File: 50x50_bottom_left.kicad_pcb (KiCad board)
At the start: 2 copper layers, 48.9 x 48.3 mm, 103 parts, among them CON1 BARREL_JACK, J1 INTERCONNECT_1X03, J10 INTERCONNECT_1X03, J11 INTERCONNECT_1X03, J12 INTERCONNECT_1X03, J13 INTERCONNECT_1X03, J14 INTERCONNECT_1X03, J15 INTERCONNECT_1X03, J16 INTERCONNECT_1X03, J17 INTERCONNECT_1X03, J18 INTERCONNECT_1X03, J19 INTERCONNECT_1X03, J2 INTERCONNECT_1X03, J20 INTERCONNECT_1X03, J21 INTERCONNECT_1X03, J22 INTERCONNECT_1X03, J23 INTERCONNECT_1X03, J24 INTERCONNECT_1X03, J25 INTERCONNECT_1X03, J26 INTERCONNECT_1X03, J27 INTERCONNECT_1X03, J28 INTERCONNECT_1X03, J29 INTERCONNECT_1X03, J3 INTERCONNECT_1X03, J30 INTERCONNECT_1X03, J31 INTERCONNECT_1X03, J32 INTERCONNECT_1X03, J33 INTERCONNECT_1X03, J34 INTERCONNECT_1X03, J35 INTERCONNECT_1X03, J36 INTERCONNECT_1X03, J37 INTERCONNECT_1X03, J38 INTERCONNECT_1X03, J39 INTERCONNECT_1X03, J4 INTERCONNECT_1X03, J40 INTERCONNECT_1X03, J41 INTERCONNECT_1X03, J42 INTERCONNECT_1X03, J43 INTERCONNECT_1X03, J44 INTERCONNECT_1X03, J45 INTERCONNECT_1X03, J46 INTERCONNECT_1X03, J47 INTERCONNECT_1X03, J48 INTERCONNECT_1X03, J49 INTERCONNECT_1X03, J5 INTERCONNECT_1X03, J50 INTERCONNECT_1X03, J51 INTERCONNECT_1X03, J52 INTERCONNECT_1X03, J53 INTERCONNECT_1X03, J54 INTERCONNECT_1X03, J55 INTERCONNECT_1X03, J56 INTERCONNECT_1X03, J57 INTERCONNECT_1X03, J58 INTERCONNECT_1X03, J59 INTERCONNECT_1X03, J6 INTERCONNECT_1X03, J60 INTERCONNECT_1X03, J61 INTERCONNECT_1X03, J62 INTERCONNECT_1X03, J63 INTERCONNECT_1X03, J64 INTERCONNECT_1X03, J65 INTERCONNECT_1X02, J7 INTERCONNECT_1X03, J8 INTERCONNECT_1X03, J9 INTERCONNECT_1X03, P1 CONN_8X2, P2 CONN_8X2, U1 LM7805CT

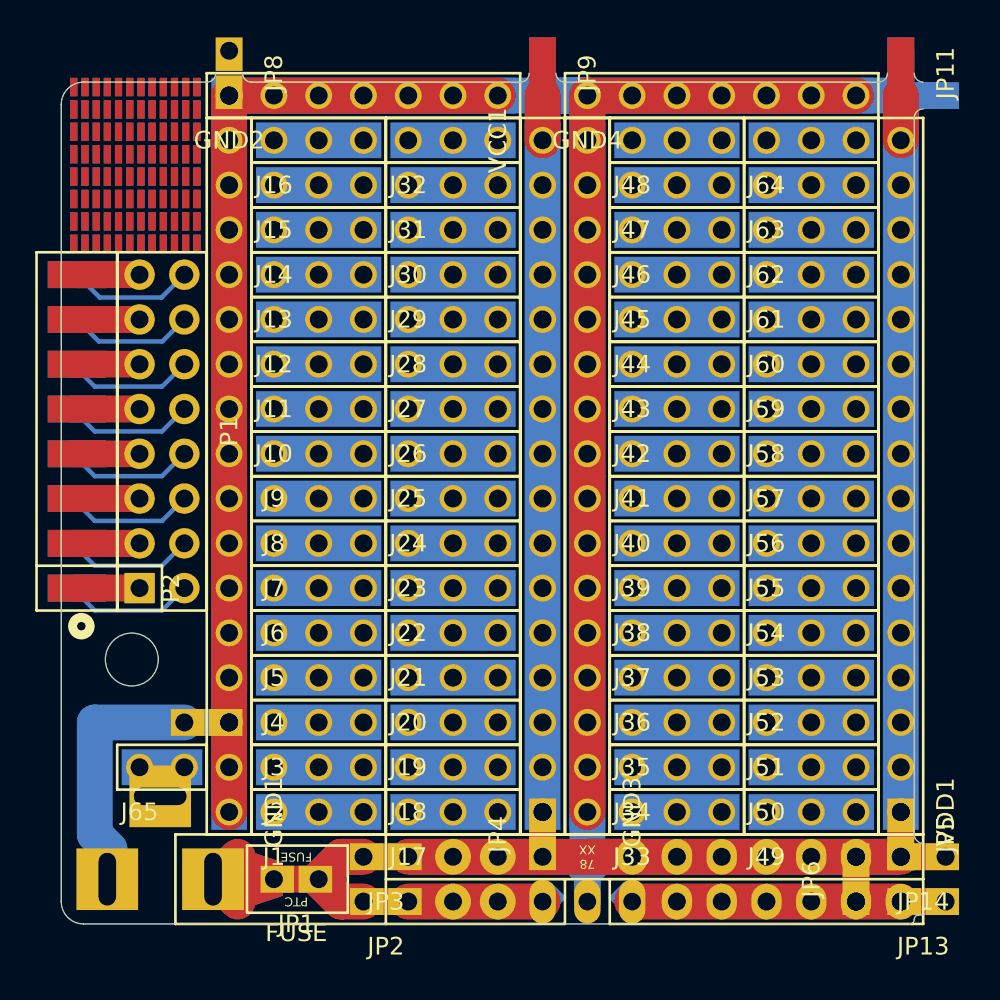
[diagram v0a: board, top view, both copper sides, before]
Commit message: added 3*3 mouse bites between the sub-boards on both edges
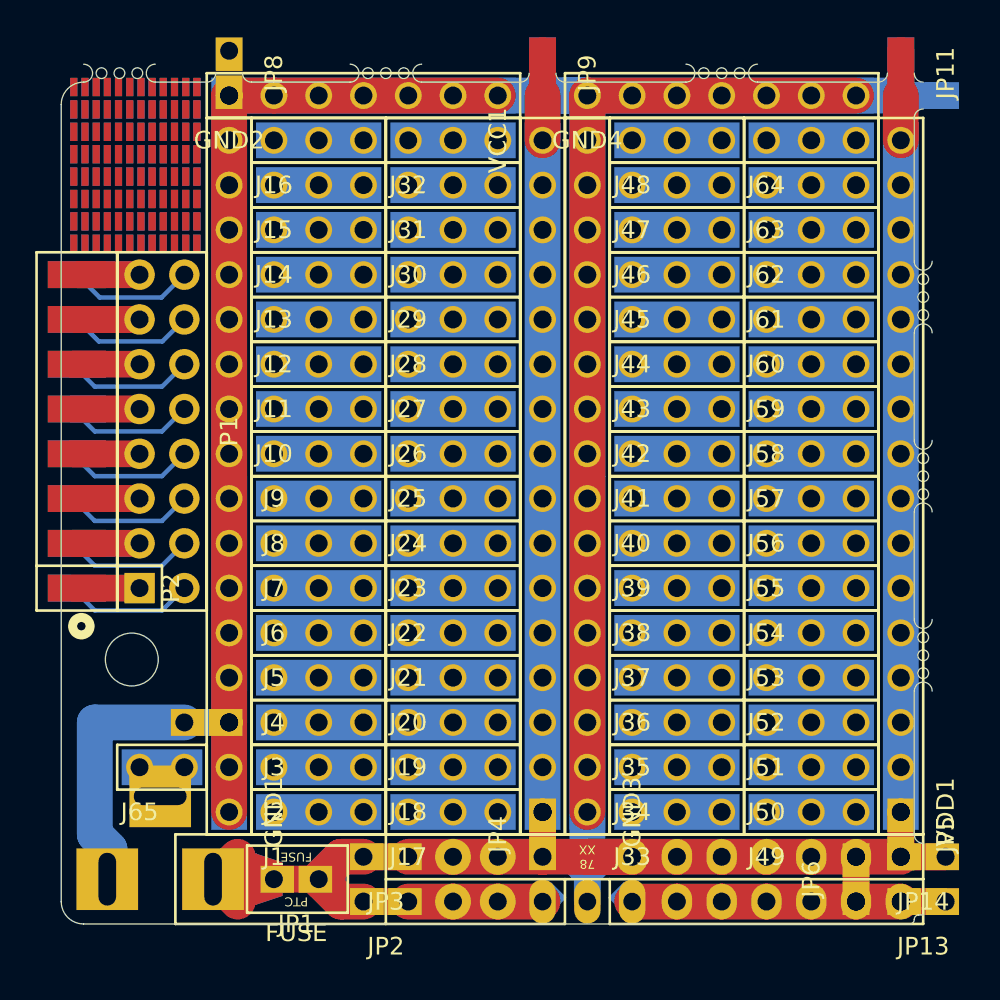
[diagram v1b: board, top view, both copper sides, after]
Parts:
- added Mouse_Bites_3_1.27mm: VAL**, Misc:Mouse_Bites_3_1.016mm, F.Cu at (44.8, 29.2)
- added Mouse_Bites_3_1.27mm: VAL**, Misc:Mouse_Bites_3_1.016mm, F.Cu at (91.4, 63.2)
- added Mouse_Bites_3_1.27mm: VAL**, Misc:Mouse_Bites_3_1.016mm, F.Cu at (91.4, 53.1)
- added Mouse_Bites_3_1.27mm: VAL**, Misc:Mouse_Bites_3_1.016mm, F.Cu at (91.4, 42.9)
- added Mouse_Bites_3_1.27mm: VAL**, Misc:Mouse_Bites_3_1.016mm, F.Cu at (79.0, 29.2)
- added Mouse_Bites_3_1.27mm: VAL**, Misc:Mouse_Bites_3_1.016mm, F.Cu at (59.9, 29.2)
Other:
- outline, holes or cut-outs redrawn
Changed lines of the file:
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@@
     (links 341)
     (no_connects 6)
-    (area 34.144048 26.7335 95.967572 82.309)
+    (area 34.144048 26.231 98.754715 82.309)
     (thickness 1.6)
-    (drawings 54)
+    (drawings 59)
     (tracks 88)
     (zones 0)
-    (modules 103)
+    (modules 109)
     (nets 99)
   )
@@
     (mod_text_size 1 1)
     (mod_text_width 0.15)
-    (pad_size 1.7272 2.032)
-    (pad_drill 1.016)
+    (pad_size 0.6096 0.6096)
+    (pad_drill 0.6096)
     (pad_to_mask_clearance 0)
     (aux_axis_origin 0 0)
@@
     )
   )
+  (module Misc:Mouse_Bites_3_1.016mm (layer F.Cu)
+    (at 44.831 29.21)
+    (fp_text reference Mouse_Bites_3_1.27mm (at 0 -1.8) (layer F.SilkS) hide
+      (effects (font (size 1 1) (thickness 0.15)))
+    )
+    (fp_text value VAL** (at 0 1.55) (layer F.SilkS) hide
+      (effects (font (size 1 1) (thickness 0.15)))
+    )
+    (fp_arc (start -1.016 0) (end -1.016 -0.508) (angle 180) (layer Edge.Cuts) (width 0.0254))
+    (fp_arc (start 3.048 0) (end 3.048 0.508) (angle 180) (layer Edge.Cuts) (width 0.0254))
+    (pad "" np_thru_hole circle (at 2.032 0) (size 0.6096 0.6096) (drill 0.6096) (layers *.Cu *.Mask F.SilkS)
+      (clearance 0.2032))
+    (pad "" np_thru_hole circle (at 1.016 0) (size 0.6096 0.6096) (drill 0.6096) (layers *.Cu *.Mask F.SilkS)
+      (clearance 0.2032))
+    (pad "" np_thru_hole circle (at 0 0) (size 0.6096 0.6096) (drill 0.6096) (layers *.Cu *.Mask F.SilkS)
+      (clearance 0.2032))
+  )
+  (module Misc:Mouse_Bites_3_1.016mm (layer F.Cu)
+    (at 91.44 63.246 90)
+    (fp_text reference Mouse_Bites_3_1.27mm (at 0 -1.8 90) (layer F.SilkS) hide
+      (effects (font (size 1 1) (thickness 0.15)))
+    )
+    (fp_text value VAL** (at 0 1.55 90) (layer F.SilkS) hide
+      (effects (font (size 1 1) (thickness 0.15)))
+    )
+    (fp_arc (start -1.016 0) (end -1.016 -0.508) (angle 180) (layer Edge.Cuts) (width 0.0254))
+    (fp_arc (start 3.048 0) (end 3.048 0.508) (angle 180) (layer Edge.Cuts) (width 0.0254))
+    (pad "" np_thru_hole circle (at 2.032 0 90) (size 0.6096 0.6096) (drill 0.6096) (layers *.Cu *.Mask F.SilkS)
+      (clearance 0.2032))
+    (pad "" np_thru_hole circle (at 1.016 0 90) (size 0.6096 0.6096) (drill 0.6096) (layers *.Cu *.Mask F.SilkS)
+      (clearance 0.2032))
+    (pad "" np_thru_hole circle (at 0 0 90) (size 0.6096 0.6096) (drill 0.6096) (layers *.Cu *.Mask F.SilkS)
+      (clearance 0.2032))
+  )
+  (module Misc:Mouse_Bites_3_1.016mm (layer F.Cu)
+    (at 91.44 53.086 90)
+    (fp_text reference Mouse_Bites_3_1.27mm (at 0 -1.8 90) (layer F.SilkS) hide
+      (effects (font (size 1 1) (thickness 0.15)))
+    )
+    (fp_text value VAL** (at 0 1.55 90) (layer F.SilkS) hide
+      (effects (font (size 1 1) (thickness 0.15)))
+    )
+    (fp_arc (start -1.016 0) (end -1.016 -0.508) (angle 180) (layer Edge.Cuts) (width 0.0254))
+    (fp_arc (start 3.048 0) (end 3.048 0.508) (angle 180) (layer Edge.Cuts) (width 0.0254))
+    (pad "" np_thru_hole circle (at 2.032 0 90) (size 0.6096 0.6096) (drill 0.6096) (layers *.Cu *.Mask F.SilkS)
+      (clearance 0.2032))
+    (pad "" np_thru_hole circle (at 1.016 0 90) (size 0.6096 0.6096) (drill 0.6096) (layers *.Cu *.Mask F.SilkS)
+      (clearance 0.2032))
+    (pad "" np_thru_hole circle (at 0 0 90) (size 0.6096 0.6096) (drill 0.6096) (layers *.Cu *.Mask F.SilkS)
+      (clearance 0.2032))
+  )
+  (module Misc:Mouse_Bites_3_1.016mm (layer F.Cu)
+    (at 91.44 42.926 90)
+    (fp_text reference Mouse_Bites_3_1.27mm (at 0 -1.8 90) (layer F.SilkS) hide
+      (effects (font (size 1 1) (thickness 0.15)))
+    )
+    (fp_text value VAL** (at 0 1.55 90) (layer F.SilkS) hide
+      (effects (font (size 1 1) (thickness 0.15)))
+    )
+    (fp_arc (start -1.016 0) (end -1.016 -0.508) (angle 180) (layer Edge.Cuts) (width 0.0254))
+    (fp_arc (start 3.048 0) (end 3.048 0.508) (angle 180) (layer Edge.Cuts) (width 0.0254))
+    (pad "" np_thru_hole circle (at 2.032 0 90) (size 0.6096 0.6096) (drill 0.6096) (layers *.Cu *.Mask F.SilkS)
+      (clearance 0.2032))
+    (pad "" np_thru_hole circle (at 1.016 0 90) (size 0.6096 0.6096) (drill 0.6096) (layers *.Cu *.Mask F.SilkS)
+      (clearance 0.2032))
+    (pad "" np_thru_hole circle (at 0 0 90) (size 0.6096 0.6096) (drill 0.6096) (layers *.Cu *.Mask F.SilkS)
+      (clearance 0.2032))
+  )
+  (module Misc:Mouse_Bites_3_1.016mm (layer F.Cu)
+    (at 78.994 29.21)
+    (fp_text reference Mouse_Bites_3_1.27mm (at 0 -1.8) (layer F.SilkS) hide
+      (effects (font (size 1 1) (thickness 0.15)))
+    )
+    (fp_text value VAL** (at 0 1.55) (layer F.SilkS) hide
+      (effects (font (size 1 1) (thickness 0.15)))
+    )
+    (fp_arc (start -1.016 0) (end -1.016 -0.508) (angle 180) (layer Edge.Cuts) (width 0.0254))
+    (fp_arc (start 3.048 0) (end 3.048 0.508) (angle 180) (layer Edge.Cuts) (width 0.0254))
+    (pad "" np_thru_hole circle (at 2.032 0) (size 0.6096 0.6096) (drill 0.6096) (layers *.Cu *.Mask F.SilkS)
+      (clearance 0.2032))
+    (pad "" np_thru_hole circle (at 1.016 0) (size 0.6096 0.6096) (drill 0.6096) (layers *.Cu *.Mask F.SilkS)
+      (clearance 0.2032))
+    (pad "" np_thru_hole circle (at 0 0) (size 0.6096 0.6096) (drill 0.6096) (layers *.Cu *.Mask F.SilkS)
+      (clearance 0.2032))
+  )
+  (module Misc:Mouse_Bites_3_1.016mm (layer F.Cu)
+    (at 59.944 29.21)
+    (fp_text reference Mouse_Bites_3_1.27mm (at 0 -1.8) (layer F.SilkS) hide
+      (effects (font (size 1 1) (thickness 0.15)))
+    )
+    (fp_text value VAL** (at 0 1.55) (layer F.SilkS) hide
+      (effects (font (size 1 1) (thickness 0.15)))
+    )
+    (fp_arc (start -1.016 0) (end -1.016 -0.508) (angle 180) (layer Edge.Cuts) (width 0.0254))
+    (fp_arc (start 3.048 0) (end 3.048 0.508) (angle 180) (layer Edge.Cuts) (width 0.0254))
+    (pad "" np_thru_hole circle (at 2.032 0) (size 0.6096 0.6096) (drill 0.6096) (layers *.Cu *.Mask F.SilkS)
+      (clearance 0.2032))
+    (pad "" np_thru_hole circle (at 1.016 0) (size 0.6096 0.6096) (drill 0.6096) (layers *.Cu *.Mask F.SilkS)
+      (clearance 0.2032))
+    (pad "" np_thru_hole circle (at 0 0) (size 0.6096 0.6096) (drill 0.6096) (layers *.Cu *.Mask F.SilkS)
+      (clearance 0.2032))
+  )
+  (gr_line (start 90.932 60.198) (end 90.932 54.102) (angle 90) (layer Edge.Cuts) (width 0.0254))
+  (gr_line (start 90.932 64.262) (end 90.932 72.39) (angle 90) (layer Edge.Cuts) (width 0.0254))
+  (gr_line (start 90.932 43.942) (end 90.932 50.038) (angle 90) (layer Edge.Cuts) (width 0.0254))
+  (gr_line (start 90.932 31.75) (end 90.932 39.878) (angle 90) (layer Edge.Cuts) (width 0.0254))
+  (gr_line (start 82.042 29.718) (end 88.9 29.718) (angle 90) (layer Edge.Cuts) (width 0.0254))
+  (gr_line (start 71.12 29.718) (end 77.978 29.718) (angle 90) (layer Edge.Cuts) (width 0.0254))
+  (gr_line (start 62.992 29.718) (end 68.58 29.718) (angle 90) (layer Edge.Cuts) (width 0.0254))
+  (gr_line (start 53.34 29.718) (end 58.928 29.718) (angle 90) (layer Edge.Cuts) (width 0.0254))
+  (gr_line (start 47.879 29.718) (end 50.8 29.718) (angle 90) (layer Edge.Cuts) (width 0.0254))
   (gr_line (start 73.66 74.93) (end 73.66 77.47) (angle 90) (layer F.SilkS) (width 0.15))
   (gr_text 330n (at 71.501 73.279 225) (layer B.SilkS)
@@
   (gr_arc (start 90.678 77.216) (end 90.932 77.216) (angle 90) (layer Edge.Cuts) (width 0.0254))
   (gr_arc (start 91.186 77.216) (end 90.932 77.216) (angle 90) (layer Edge.Cuts) (width 0.0254))
-  (gr_line (start 43.815 29.718) (end 50.8 29.718) (angle 90) (layer Edge.Cuts) (width 0.0254))
   (gr_arc (start 43.815 30.988) (end 42.545 30.988) (angle 90) (layer Edge.Cuts) (width 0.0254))
   (gr_line (start 91.44 72.39) (end 49.022 72.39) (angle 90) (layer F.SilkS) (width 0.15))
   (gr_arc (start 50.8 29.21) (end 50.8 29.718) (angle -90) (layer Edge.Cuts) (width 0.0254))
   (gr_arc (start 53.34 29.21) (end 52.832 29.21) (angle -90) (layer Edge.Cuts) (width 0.0254))
-  (gr_line (start 68.58 29.718) (end 53.34 29.718) (angle 90) (layer Edge.Cuts) (width 0.0254))
   (gr_arc (start 68.58 29.21) (end 68.58 29.718) (angle -90) (layer Edge.Cuts) (width 0.0254))
   (gr_arc (start 71.12 29.21) (end 70.612 29.21) (angle -90) (layer Edge.Cuts) (width 0.0254))
-  (gr_line (start 88.9 29.718) (end 71.12 29.718) (angle 90) (layer Edge.Cuts) (width 0.0254))
   (gr_arc (start 88.9 29.21) (end 88.9 29.718) (angle -90) (layer Edge.Cuts) (width 0.0254))
   (gr_arc (start 91.44 29.21) (end 90.932 29.21) (angle -90) (layer Edge.Cuts) (width 0.0254))
   (gr_arc (start 91.44 31.75) (end 91.44 31.242) (angle -90) (layer Edge.Cuts) (width 0.0254))
-  (gr_line (start 90.932 72.39) (end 90.932 31.75) (angle 90) (layer Edge.Cuts) (width 0.0254))
   (gr_arc (start 91.44 72.39) (end 90.932 72.39) (angle -90) (layer Edge.Cuts) (width 0.0254))
   (gr_arc (start 43.815 76.2) (end 42.545 76.2) (angle -90) (layer Edge.Cuts) (width 0.0254))
